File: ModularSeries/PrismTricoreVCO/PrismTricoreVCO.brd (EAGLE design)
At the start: 88 x 49 mm, 58 parts, among them Q1 2N3906, Q2 2N3906

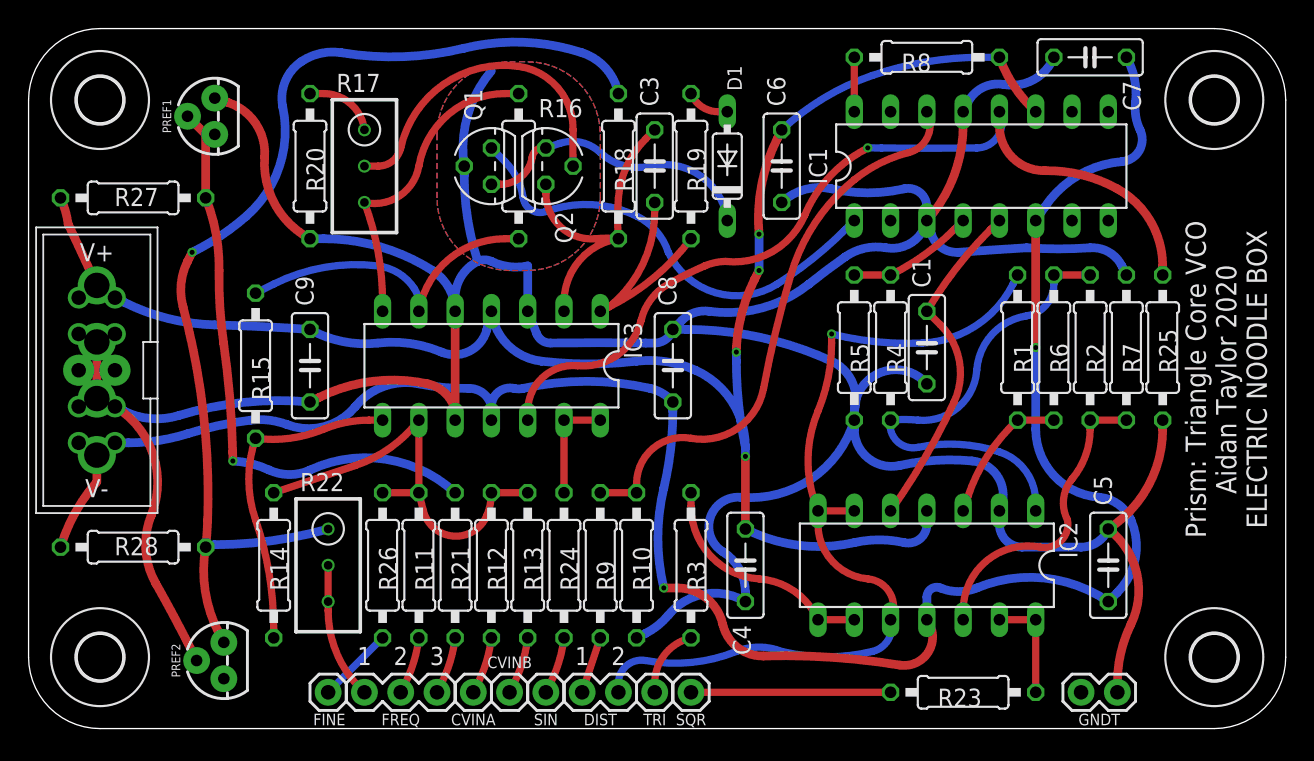
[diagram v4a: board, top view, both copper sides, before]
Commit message: Documentation updated for Prism and Portals for new power header
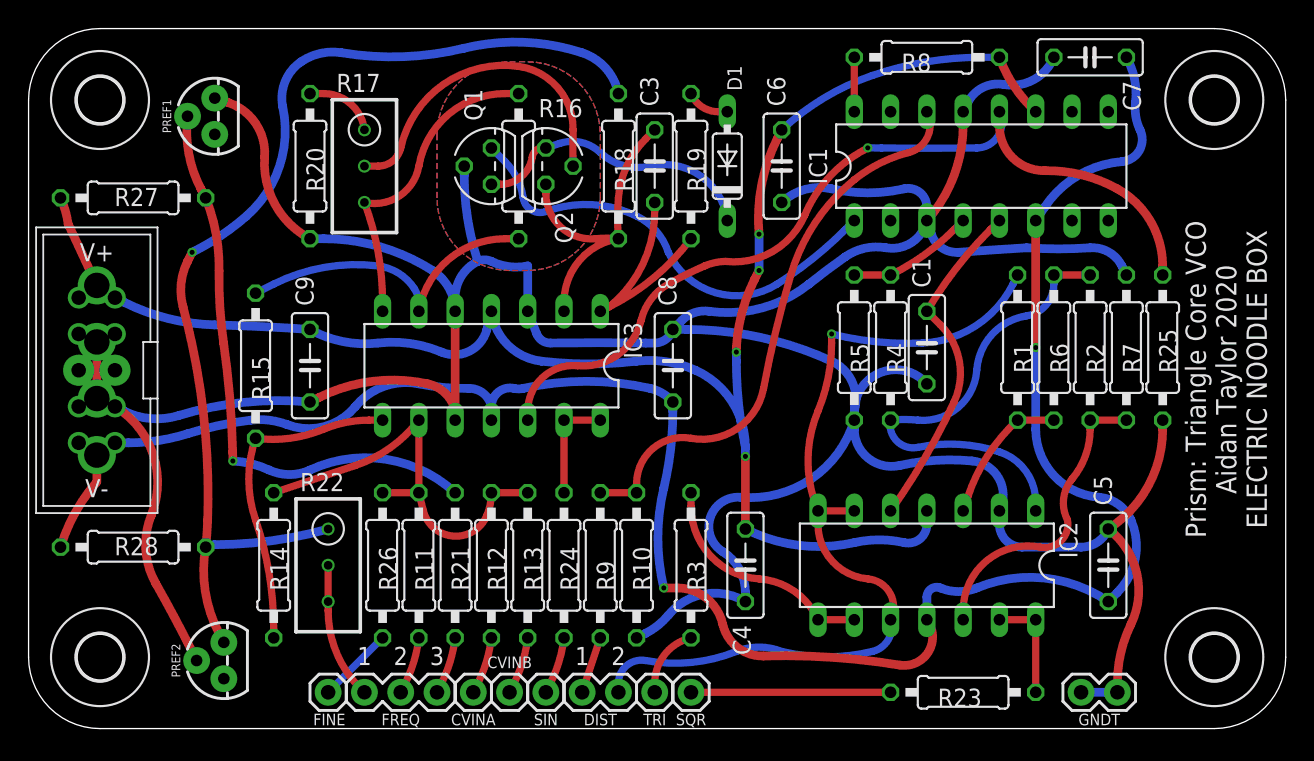
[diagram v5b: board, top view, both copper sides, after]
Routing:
- net AGND: track 278.8 -> 275.0 mm
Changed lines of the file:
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@@
 <wire x1="57.165" y1="33.02" x2="60.0225" y2="33.655" width="0.6096" layer="16" curve="-45.141346"/>
 <wire x1="60.0225" y1="33.655" x2="62.88" y2="35.56" width="0.6096" layer="16" curve="87.463877"/>
-<wire x1="32.4" y1="46.0375" x2="30.495" y2="39.37" width="0.6096" layer="16" curve="48.670313"/>
 <wire x1="30.495" y1="39.37" x2="30.495" y2="38.735" width="0.6096" layer="16"/>
 <wire x1="30.495" y1="38.735" x2="31.4475" y2="32.7025" width="0.6096" layer="16" curve="17.945254"/>
@@
 <wire x1="4.7775" y1="27.0625" x2="6.0475" y2="27.6225" width="0.6096" layer="1"/>
 <wire x1="4.7775" y1="27.0625" x2="4.7775" y2="23.1025" width="0.6096" layer="1"/>
-<wire x1="76.215" y1="3.175" x2="76.215" y2="2.54" width="0" layer="19" extent="1-1"/>
-<wire x1="73.675" y1="2.54" x2="76.215" y2="2.54" width="0" layer="19" extent="1-1"/>
+<wire x1="73.675" y1="2.54" x2="76.215" y2="2.54" width="0.6096" layer="16"/>
+<wire x1="76.215" y1="2.54" x2="76.215" y2="3.175" width="0.6096" layer="1"/>
 </signal>
 <signal name="N$4">
@@
 <contactref element="PREF1" pad="2"/>
 <contactref element="R27" pad="1"/>
-<wire x1="12.3975" y1="41.5925" x2="11.1275" y2="42.8625" width="0.6096" layer="1"/>
-<wire x1="12.3975" y1="41.5925" x2="12.3975" y2="37.1475" width="0.6096" layer="1"/>
 <wire x1="16.8425" y1="18.0975" x2="14.3025" y2="18.7325" width="0.6096" layer="16" curve="21.895634"/>
 <via x="14.3025" y="18.7325" extent="1-16" drill="0.35"/>
@@
 <wire x1="13.6525" y1="26.9875" x2="13.335" y2="32.0675" width="0.6096" layer="1" curve="-9.195468"/>
 <wire x1="13.335" y1="32.0675" x2="12.3975" y2="37.1475" width="0.6096" layer="1" curve="22.955086"/>
+<wire x1="12.3975" y1="37.1475" x2="12.065" y2="37.7825" width="0.6096" layer="1"/>
+<wire x1="12.065" y1="37.7825" x2="11.1275" y2="42.8625" width="0.6096" layer="1" curve="-34.362827"/>
 </signal>
 <signal name="-10VREF">

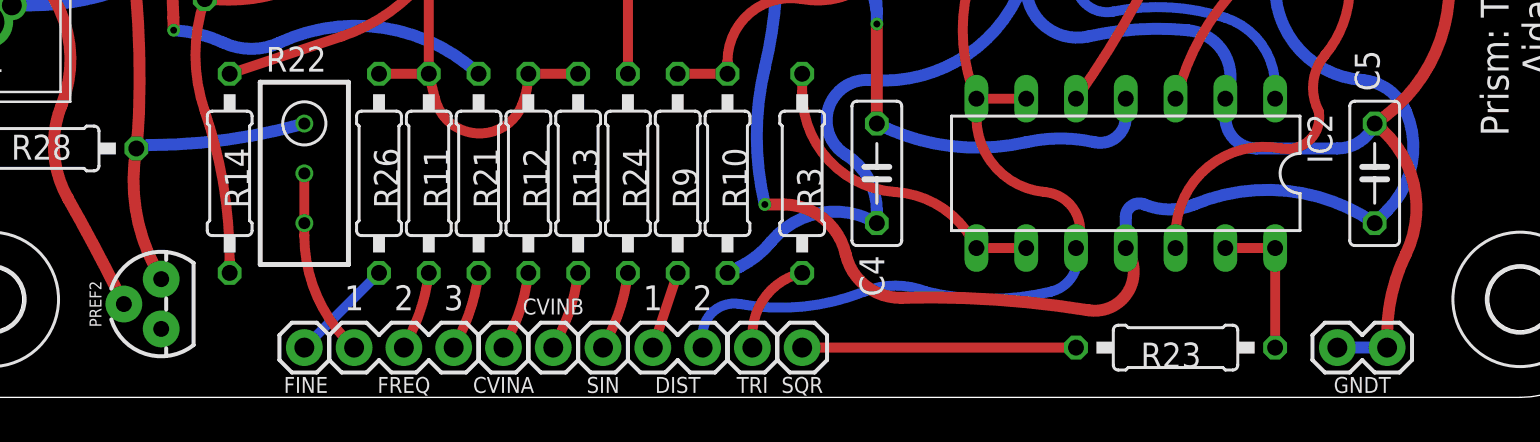
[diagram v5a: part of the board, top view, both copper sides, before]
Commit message: Control PCBs for Prism, Portals, TimeSeeds and Knives added
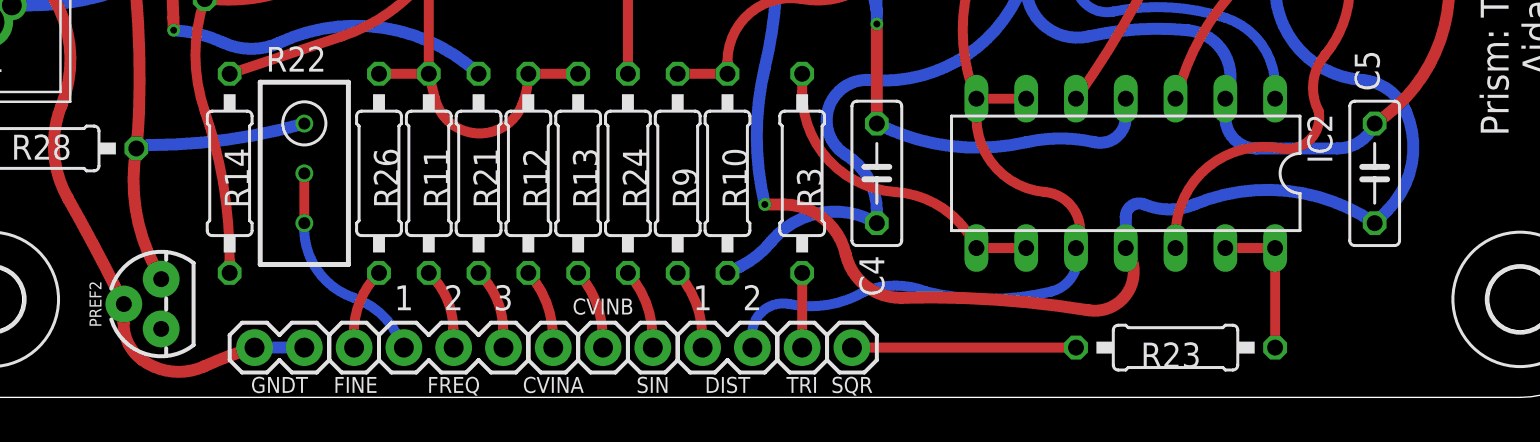
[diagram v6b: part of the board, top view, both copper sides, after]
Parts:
- moved GNDT 55.2 mm to (18.4, 2.54)
- moved CVINA 2.54 mm to (33.7, 2.54)
- moved FINE 2.54 mm to (23.5, 2.54)
- moved CVINB 2.54 mm to (36.2, 2.54)
- moved DIST 2.54 mm to (41.3, 2.54)
- moved FREQ 2.54 mm to (26.1, 2.54)
- moved SIN 2.54 mm to (38.8, 2.54)
- moved SQR 2.54 mm to (48.9, 2.54)
- moved TRI 2.54 mm to (46.4, 2.54)
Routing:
- net AGND: track 275.0 -> 272.3 mm
- net N$30: track 14.0 -> 11.4 mm
- net N$1: track 60.7 -> 58.1 mm
- net N$32: track 5.39 -> 4.06 mm
- net N$25: track 9.43 -> 10.8 mm
- net N$29: track 4.70 -> 3.81 mm

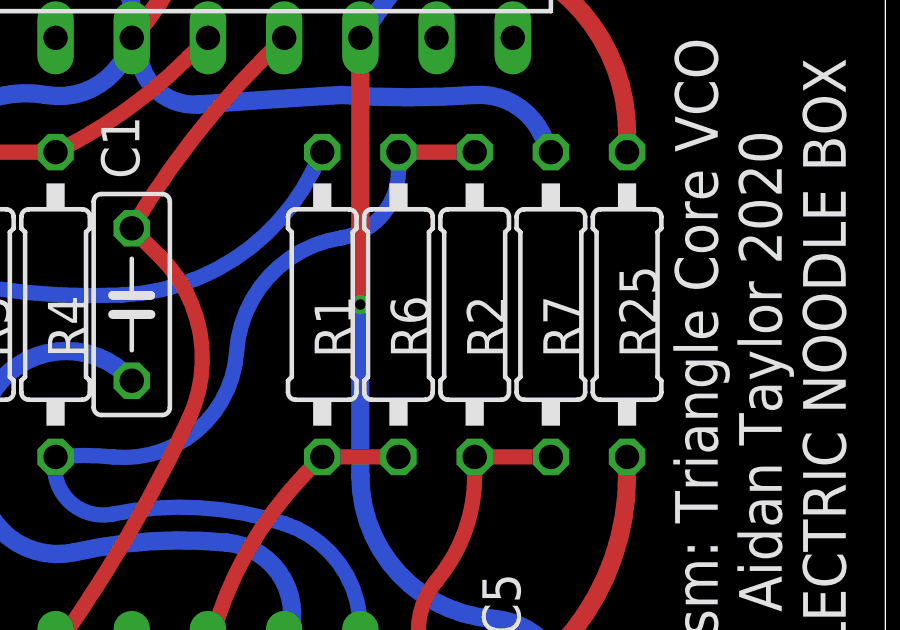
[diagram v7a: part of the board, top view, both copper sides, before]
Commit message: Prism updates, silkscreen errors fixed, resistor values updated, BOM updated
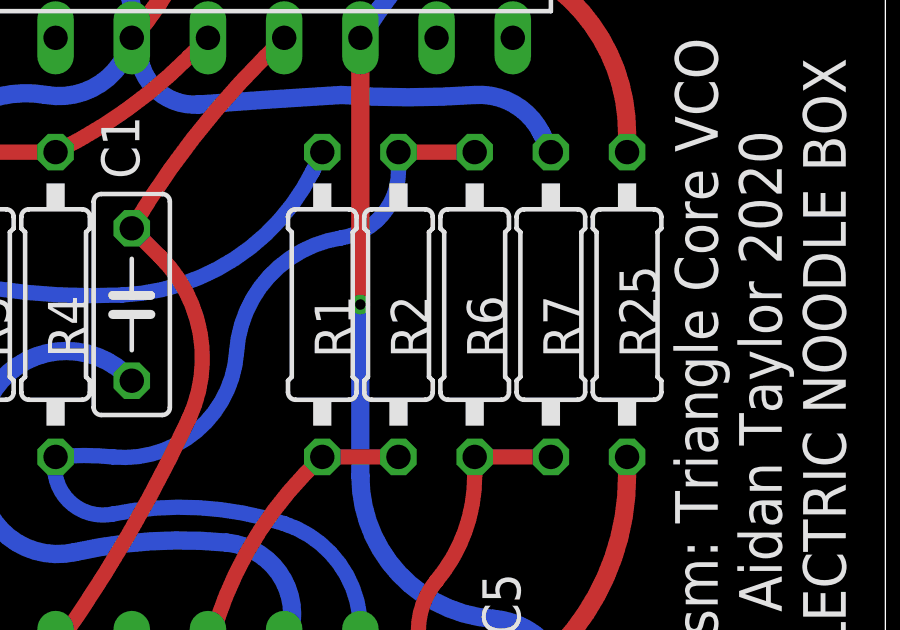
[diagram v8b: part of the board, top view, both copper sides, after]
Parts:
- R10: value 10K -> 1K
- R27, R28, R9: value 10K -> 4K7
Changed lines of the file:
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@@
 <attribute name="VALUE" x="69.865" y="24.4094" size="1.27" layer="27" ratio="10" rot="R90"/>
 </element>
-<element name="R10" library="rcl" library_urn="urn:adsk.eagle:library:334" package="0207/10" package3d_urn="urn:adsk.eagle:package:23491/2" value="10K" x="42.56" y="11.43" smashed="yes" rot="R90">
+<element name="R10" library="rcl" library_urn="urn:adsk.eagle:library:334" package="0207/10" package3d_urn="urn:adsk.eagle:package:23491/2" value="1K" x="42.56" y="11.43" smashed="yes" rot="R90">
 <attribute name="NAME" x="43.576" y="9.652" size="1.27" layer="25" ratio="10" rot="R90"/>
 <attribute name="POPULARITY" value="81" x="92.09" y="43.18" size="1.778" layer="27" rot="R90" display="off"/>
@@
 </element>
 <element name="R2" library="rcl" library_urn="urn:adsk.eagle:library:334" package="0207/10" package3d_urn="urn:adsk.eagle:package:23491/2" value="22K" x="71.77" y="26.67" smashed="yes" rot="R270">
-<attribute name="NAME" x="75.326" y="24.892" size="1.27" layer="25" ratio="10" rot="R90"/>
+<attribute name="NAME" x="72.786" y="24.892" size="1.27" layer="25" ratio="10" rot="R90"/>
 <attribute name="POPULARITY" value="81" x="32.4" y="-5.08" size="1.778" layer="27" rot="R270" display="off"/>
 <attribute name="SPICEPREFIX" value="R" x="32.4" y="-5.08" size="1.778" layer="27" rot="R270" display="off"/>
@@
 </element>
 <element name="R6" library="rcl" library_urn="urn:adsk.eagle:library:334" package="0207/10" package3d_urn="urn:adsk.eagle:package:23491/2" value="100K" x="74.31" y="26.67" smashed="yes" rot="R90">
-<attribute name="NAME" x="72.786" y="24.892" size="1.27" layer="25" ratio="10" rot="R90"/>
+<attribute name="NAME" x="75.326" y="24.892" size="1.27" layer="25" ratio="10" rot="R90"/>
 <attribute name="POPULARITY" value="81" x="118.76" y="58.42" size="1.778" layer="27" rot="R90" display="off"/>
 <attribute name="SPICEPREFIX" value="R" x="118.76" y="58.42" size="1.778" layer="27" rot="R90" display="off"/>
@@
 <attribute name="VALUE" x="65.1406" y="47.625" size="1.27" layer="27" ratio="10" rot="R180"/>
 </element>
-<element name="R9" library="rcl" library_urn="urn:adsk.eagle:library:334" package="0207/10" package3d_urn="urn:adsk.eagle:package:23491/2" value="10K" x="40.02" y="11.43" smashed="yes" rot="R90">
+<element name="R9" library="rcl" library_urn="urn:adsk.eagle:library:334" package="0207/10" package3d_urn="urn:adsk.eagle:package:23491/2" value="4K7" x="40.02" y="11.43" smashed="yes" rot="R90">
 <attribute name="NAME" x="41.036" y="9.652" size="1.27" layer="25" ratio="10" rot="R90"/>
 <attribute name="POPULARITY" value="81" x="89.55" y="30.48" size="1.778" layer="27" rot="R90" display="off"/>
@@
 <attribute name="VALUE" x="15.5725" y="4.7625" size="0.6096" layer="27" font="vector" ratio="20" rot="R90" align="top-center"/>
 </element>
-<element name="R27" library="rcl" library_urn="urn:adsk.eagle:library:334" package="0207/10" package3d_urn="urn:adsk.eagle:package:23491/2" value="10K" x="7.3175" y="37.1475" smashed="yes" rot="R180">
+<element name="R27" library="rcl" library_urn="urn:adsk.eagle:library:334" package="0207/10" package3d_urn="urn:adsk.eagle:package:23491/2" value="4K7" x="7.3175" y="37.1475" smashed="yes" rot="R180">
 <attribute name="NAME" x="9.0955" y="37.846" size="1.27" layer="25" ratio="10" rot="R180"/>
 <attribute name="POPULARITY" value="81" x="7.3175" y="37.1475" size="1.778" layer="27" rot="R180" display="off"/>
@@
 <attribute name="VALUE" x="9.5781" y="37.7825" size="1.27" layer="27" ratio="10" rot="R180"/>
 </element>
-<element name="R28" library="rcl" library_urn="urn:adsk.eagle:library:334" package="0207/10" package3d_urn="urn:adsk.eagle:package:23491/2" value="10K" x="7.3175" y="12.7" smashed="yes" rot="R180">
+<element name="R28" library="rcl" library_urn="urn:adsk.eagle:library:334" package="0207/10" package3d_urn="urn:adsk.eagle:package:23491/2" value="4K7" x="7.3175" y="12.7" smashed="yes" rot="R180">
 <attribute name="NAME" x="9.0955" y="13.3985" size="1.27" layer="25" ratio="10" rot="R180"/>
 <attribute name="POPULARITY" value="81" x="7.3175" y="12.7" size="1.778" layer="27" rot="R180" display="off"/>
